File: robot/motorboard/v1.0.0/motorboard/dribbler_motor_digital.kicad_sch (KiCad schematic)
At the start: 13 parts

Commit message: drive and dribbler modules prototype
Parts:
- removed C? (x2): 0.1uF 6.3V, symbol Device:C
- removed C?: 1uF 25V, symbol Device:C
- removed C?: 1uF 6.3V, symbol Device:C
- removed D?: RED, symbol Device:LED
- removed J?: Conn_01x06_Female, symbol Connector:Conn_01x06_Female
- removed J?: Conn_01x05_Female, symbol Connector:Conn_01x05_Female
- removed R?: 1k, symbol Device:R_US
- removed R? (x4): 10k, symbol Device:R_US
- removed U?: STSPIN32F0A, symbol st_microcontrollers:STSPIN32F0A
- added C?: 1uF 25V, symbol Device:C
- added C?: 1uF 6.3V, symbol Device:C
- added C? (x2): 0.1uF 6.3V, symbol Device:C
- added D?: BLUE, symbol Device:LED
- added D?: RED, symbol Device:LED
- added J?: Conn_01x05_Female, symbol Connector:Conn_01x05_Female
- added R? (x4): 10k, symbol Device:R_US
- added R? (x2): 1k, symbol Device:R_US
- added U?: STSPIN32F0A, symbol st_microcontrollers:STSPIN32F0A
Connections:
- net BOOT0: now also U?.42 (BOOT0)
- net GND: now also C?.2, C?.2, C?.2, C?.2, D?.1 (K), D?.1 (K), J?.5 (Pin_5), U?.20 (Test_Mode), U?.44 (GND)
- net HALL_A: now also J?.2 (Pin_2), R?.2, U?.11 (PA0/GPIO/T2C1/ADC0)
- net HALL_B: now also J?.3 (Pin_3), R?.2, U?.12 (PA1/GPIO/T2C2/ADC1)
- net HALL_C: now also J?.4 (Pin_4), R?.2, U?.13 (PA2/GPIO/USART1_TX/T2C3/ADC2)
- net LED_ERR: now also R?.1, U?.41 (PB7/GPIO/USART1_RX)
- net NRST: now also R?.2, U?.7 (NRST)
- net SENSE_U: now also U?.14 (PA3/GPIO/USART1_RX/T2C4/ADC3)
- net SENSE_V: now also U?.15 (PA4/GPIO/ADC4)
- net SENSE_W: now also U?.16 (PA5/GPIO/ADC5)
- net SWDCLK: now also U?.38 (PA14/SWDCLK/USART1_TX/BL_UART_TX)
- net SWDIO: now also U?.37 (PA13/SWDIO)
- net UART_RX: now also U?.39 (PA15/USART1_RX/BL_UART_RX)
- net VDD: now also C?.1, C?.1, R?.1, U?.48 (VDD), U?.9 (SW)
- net VDDA: now also C?.1, U?.10 (VDDA)
- net Vhall: now also J?.1 (Pin_1), R?.1, R?.1, R?.1
- new net: C?.1, U?.6 (VREG12)
- new net: D?.2 (A), R?.2 (x2)
- new net LED_BALL_DET: R?.1, U?.40 (PB6/GPIO/USART1_TX)

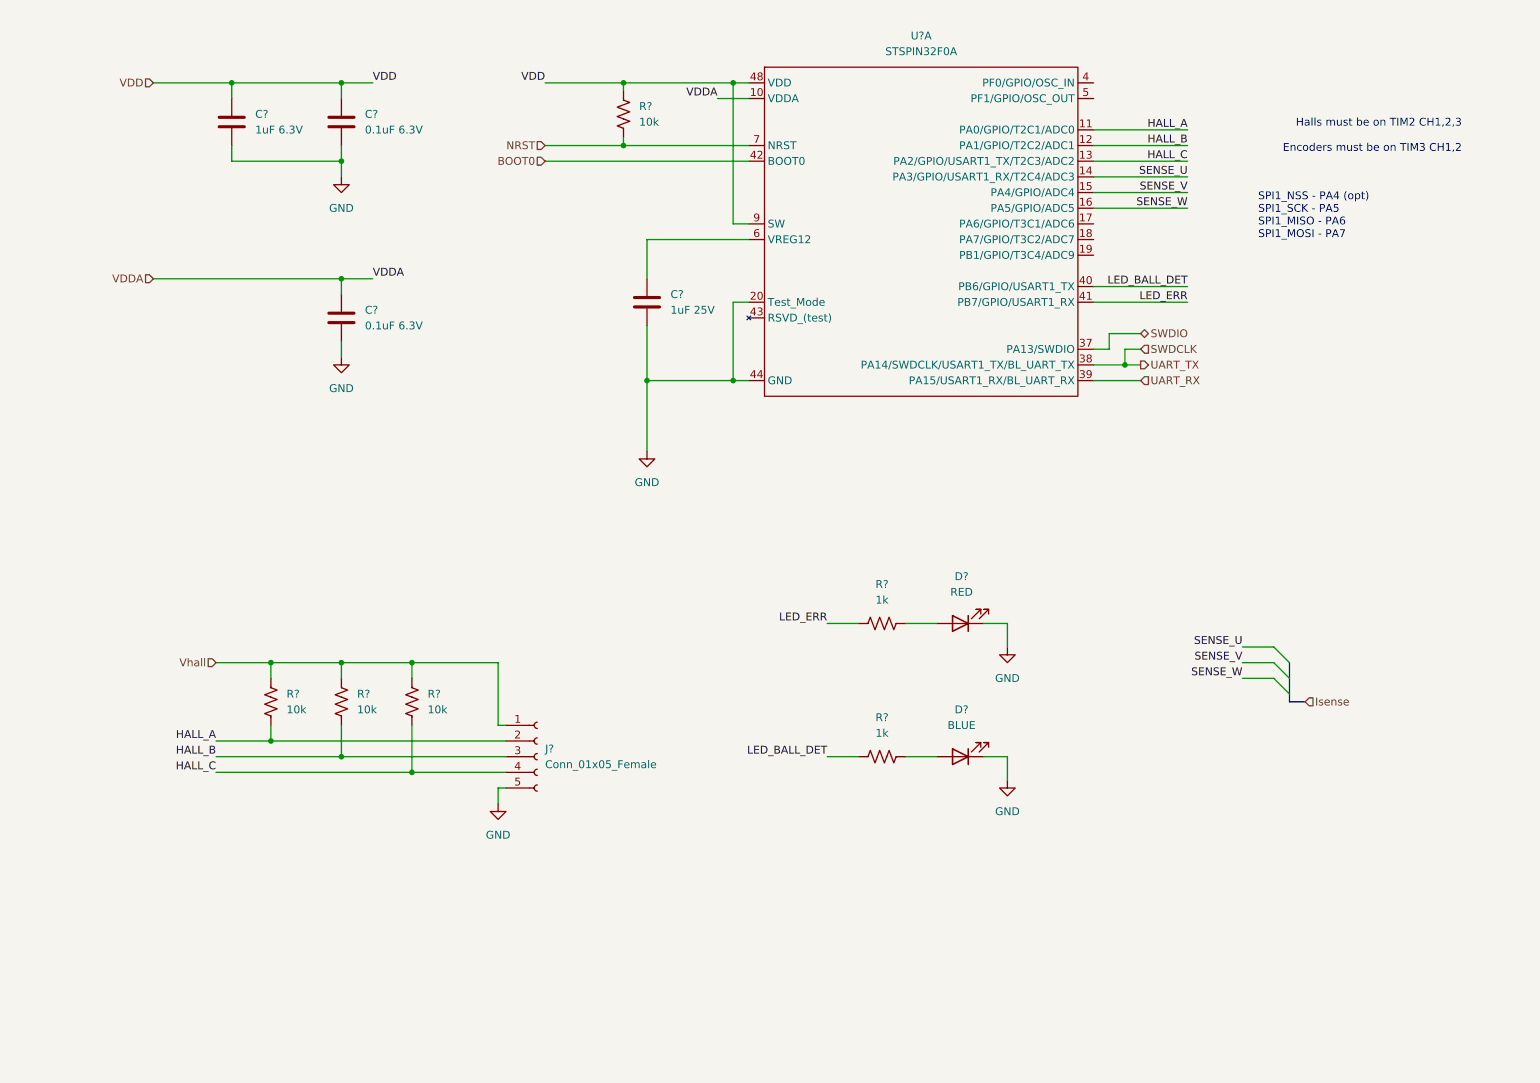
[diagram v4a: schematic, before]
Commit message: bus name ERC fixes
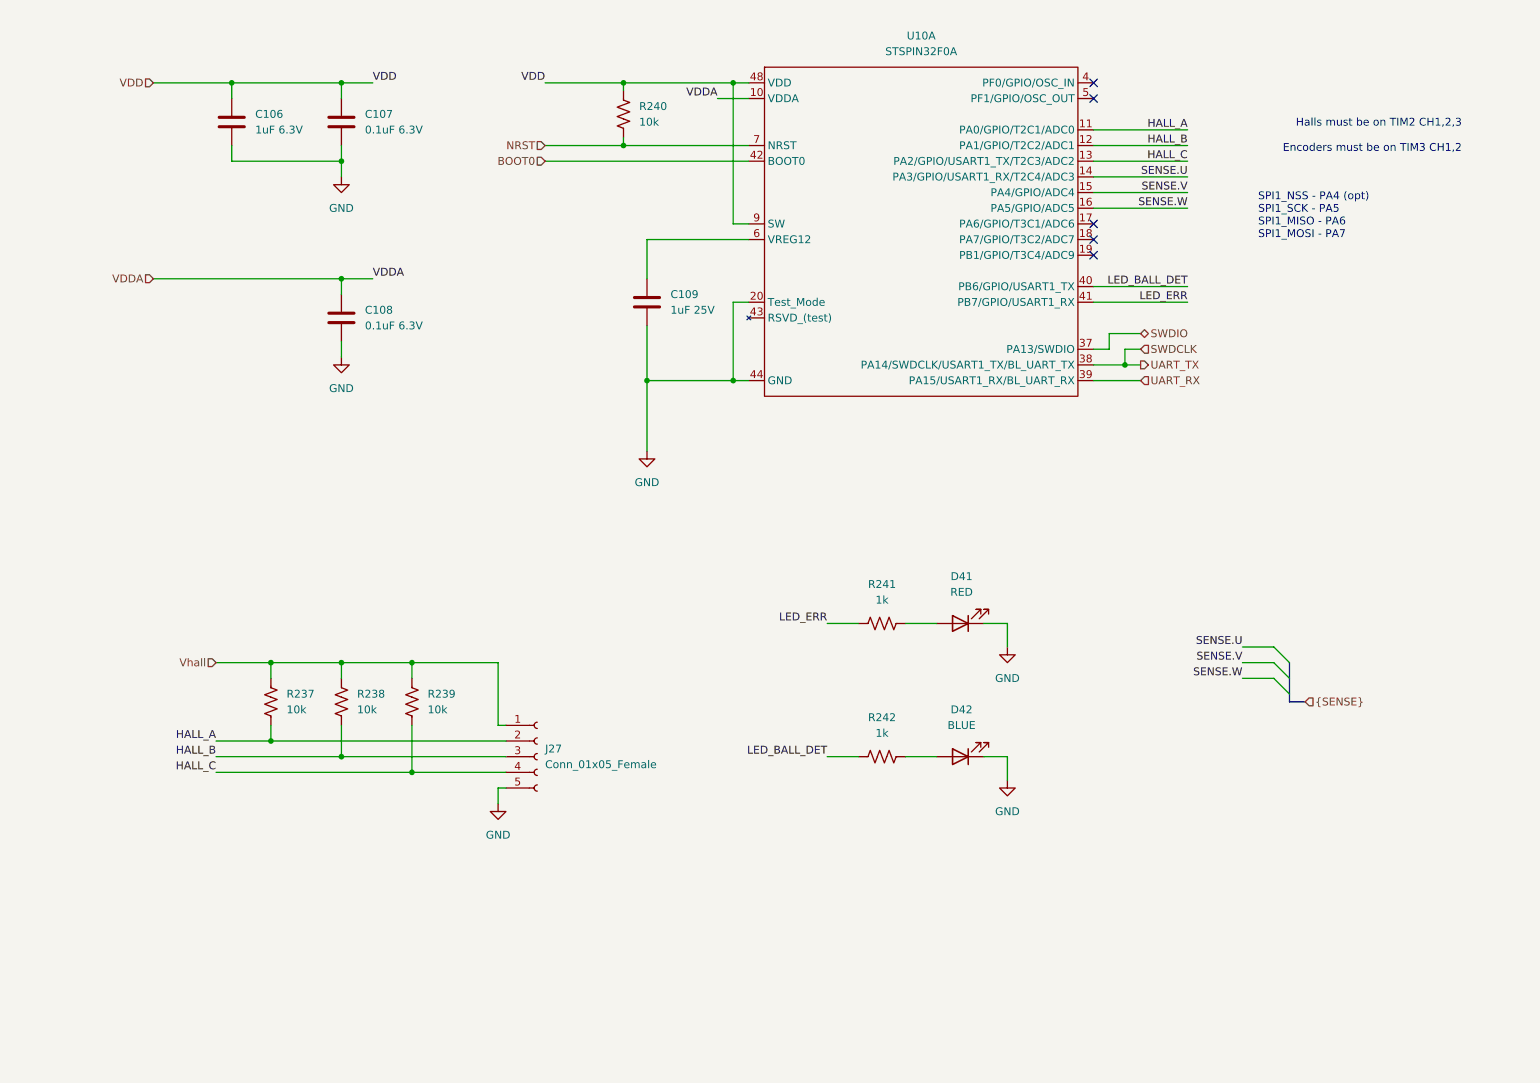
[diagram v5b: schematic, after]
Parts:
- gave numbers to parts that had none: 14
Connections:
- net SENSE_U renamed SENSE.U
- net SENSE_V renamed SENSE.V
- net SENSE_W renamed SENSE.W
- no-connect marks 0 -> 5
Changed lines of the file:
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@@
   (junction (at 135.89 78.74) (diameter 0.9144) (color 0 0 0 0))
   (junction (at 199.39 76.2) (diameter 0.9144) (color 0 0 0 0))
+  (no_connect (at 194.31 30.48))
+  (no_connect (at 194.31 33.02))
+  (no_connect (at 194.31 53.34))
+  (no_connect (at 194.31 55.88))
+  (no_connect (at 194.31 58.42))
   (bus_entry (at 223.52 121.92) (size 2.54 2.54)
     (stroke (width 0) (type solid) (color 0 0 0 0))
@@
     (effects (font (size 1.27 1.27)) (justify right bottom))
   )
-  (label "SENSE_U" (at 209.55 45.72 180)
-    (effects (font (size 1.27 1.27)) (justify right bottom))
-  )
-  (label "SENSE_V" (at 209.55 48.26 180)
-    (effects (font (size 1.27 1.27)) (justify right bottom))
-  )
-  (label "SENSE_W" (at 209.55 50.8 180)
+  (label "SENSE.U" (at 209.55 45.72 180)
+    (effects (font (size 1.27 1.27)) (justify right bottom))
+  )
+  (label "SENSE.V" (at 209.55 48.26 180)
+    (effects (font (size 1.27 1.27)) (justify right bottom))
+  )
+  (label "SENSE.W" (at 209.55 50.8 180)
     (effects (font (size 1.27 1.27)) (justify right bottom))
   )
@@
     (effects (font (size 1.27 1.27)) (justify right bottom))
   )
-  (label "SENSE_U" (at 218.44 121.92 180)
-    (effects (font (size 1.27 1.27)) (justify right bottom))
-  )
-  (label "SENSE_V" (at 218.44 124.46 180)
-    (effects (font (size 1.27 1.27)) (justify right bottom))
-  )
-  (label "SENSE_W" (at 218.44 127 180)
+  (label "SENSE.U" (at 218.44 121.92 180)
+    (effects (font (size 1.27 1.27)) (justify right bottom))
+  )
+  (label "SENSE.V" (at 218.44 124.46 180)
+    (effects (font (size 1.27 1.27)) (justify right bottom))
+  )
+  (label "SENSE.W" (at 218.44 127 180)
     (effects (font (size 1.27 1.27)) (justify right bottom))
   )
@@
     (effects (font (size 1.27 1.27)) (justify left))
   )
-  (hierarchical_label "Isense" (shape input) (at 228.6 130.81 0)
+  (hierarchical_label "{SENSE}" (shape input) (at 228.6 130.81 0)
     (effects (font (size 1.27 1.27)) (justify left))
   )
   (symbol (lib_id "power:GND") (at 72.39 45.72 0) (unit 1)
     (in_bom yes) (on_board yes)
-    (property "Reference" "#PWR?" (id 0) (at 72.39 52.07 0)
+    (property "Reference" "#PWR0160" (id 0) (at 72.39 52.07 0)
       (effects (font (size 1.27 1.27)) hide)
     )
@@
   (symbol (lib_id "power:GND") (at 72.39 74.93 0) (unit 1)
     (in_bom yes) (on_board yes) (fields_autoplaced)
-    (property "Reference" "#PWR?" (id 0) (at 72.39 81.28 0)
+    (property "Reference" "#PWR0161" (id 0) (at 72.39 81.28 0)
       (effects (font (size 1.27 1.27)) hide)
     )
@@
   (symbol (lib_id "power:GND") (at 97.79 147.32 0) (unit 1)
     (in_bom yes) (on_board yes) (fields_autoplaced)
-    (property "Reference" "#PWR?" (id 0) (at 97.79 153.67 0)
+    (property "Reference" "#PWR0162" (id 0) (at 97.79 153.67 0)
       (effects (font (size 1.27 1.27)) hide)
     )
@@
   (symbol (lib_id "power:GND") (at 121.92 90.17 0) (unit 1)
     (in_bom yes) (on_board yes) (fields_autoplaced)
-    (property "Reference" "#PWR?" (id 0) (at 121.92 96.52 0)
+    (property "Reference" "#PWR0163" (id 0) (at 121.92 96.52 0)
       (effects (font (size 1.27 1.27)) hide)
     )
@@
   (symbol (lib_id "power:GND") (at 180.34 121.92 0) (unit 1)
     (in_bom yes) (on_board yes) (fields_autoplaced)
-    (property "Reference" "#PWR?" (id 0) (at 180.34 128.27 0)
+    (property "Reference" "#PWR0164" (id 0) (at 180.34 128.27 0)
       (effects (font (size 1.27 1.27)) hide)
     )
@@
   (symbol (lib_id "power:GND") (at 180.34 143.51 0) (unit 1)
     (in_bom yes) (on_board yes) (fields_autoplaced)
-    (property "Reference" "#PWR?" (id 0) (at 180.34 149.86 0)
+    (property "Reference" "#PWR0165" (id 0) (at 180.34 149.86 0)
       (effects (font (size 1.27 1.27)) hide)
     )
@@
   (symbol (lib_id "Device:R_US") (at 60.96 130.81 0) (unit 1)
     (in_bom yes) (on_board yes) (fields_autoplaced)
-    (property "Reference" "R?" (id 0) (at 63.5 129.5399 0)
+    (property "Reference" "R237" (id 0) (at 63.5 129.5399 0)
       (effects (font (size 1.27 1.27)) (justify left))
     )
@@
   (symbol (lib_id "Device:R_US") (at 72.39 130.81 0) (unit 1)
     (in_bom yes) (on_board yes) (fields_autoplaced)
-    (property "Reference" "R?" (id 0) (at 74.93 129.5399 0)
+    (property "Reference" "R238" (id 0) (at 74.93 129.5399 0)
       (effects (font (size 1.27 1.27)) (justify left))
     )
@@
   (symbol (lib_id "Device:R_US") (at 83.82 130.81 0) (unit 1)
     (in_bom yes) (on_board yes) (fields_autoplaced)
-    (property "Reference" "R?" (id 0) (at 86.36 129.5399 0)
+    (property "Reference" "R239" (id 0) (at 86.36 129.5399 0)
       (effects (font (size 1.27 1.27)) (justify left))
     )
@@
   (symbol (lib_id "Device:R_US") (at 118.11 35.56 0) (unit 1)
     (in_bom yes) (on_board yes) (fields_autoplaced)
-    (property "Reference" "R?" (id 0) (at 120.65 34.2899 0)
+    (property "Reference" "R240" (id 0) (at 120.65 34.2899 0)
       (effects (font (size 1.27 1.27)) (justify left))
     )
@@
   (symbol (lib_id "Device:R_US") (at 160.02 118.11 90) (unit 1)
     (in_bom yes) (on_board yes) (fields_autoplaced)
-    (property "Reference" "R?" (id 0) (at 160.02 111.76 90))
+    (property "Reference" "R241" (id 0) (at 160.02 111.76 90))
     (property "Value" "1k" (id 1) (at 160.02 114.3 90))
     (property "Footprint" "" (id 2) (at 160.274 117.094 90)
@@
   (symbol (lib_id "Device:R_US") (at 160.02 139.7 90) (unit 1)
     (in_bom yes) (on_board yes) (fields_autoplaced)
-    (property "Reference" "R?" (id 0) (at 160.02 133.35 90))
+    (property "Reference" "R242" (id 0) (at 160.02 133.35 90))
     (property "Value" "1k" (id 1) (at 160.02 135.89 90))
     (property "Footprint" "" (id 2) (at 160.274 138.684 90)
@@
   (symbol (lib_id "Device:LED") (at 172.72 118.11 180) (unit 1)
     (in_bom yes) (on_board yes) (fields_autoplaced)
-    (property "Reference" "D?" (id 0) (at 172.9105 110.49 0))
+    (property "Reference" "D41" (id 0) (at 172.9105 110.49 0))
     (property "Value" "RED" (id 1) (at 172.9105 113.03 0))
     (property "Footprint" "" (id 2) (at 172.72 118.11 0)
@@
   (symbol (lib_id "Device:LED") (at 172.72 139.7 180) (unit 1)
     (in_bom yes) (on_board yes) (fields_autoplaced)
-    (property "Reference" "D?" (id 0) (at 172.9105 132.08 0))
+    (property "Reference" "D42" (id 0) (at 172.9105 132.08 0))
     (property "Value" "BLUE" (id 1) (at 172.9105 134.62 0))
     (property "Footprint" "" (id 2) (at 172.72 139.7 0)
@@
   (symbol (lib_id "Device:C") (at 54.61 36.83 0) (unit 1)
     (in_bom yes) (on_board yes) (fields_autoplaced)
-    (property "Reference" "C?" (id 0) (at 58.42 35.5599 0)
+    (property "Reference" "C106" (id 0) (at 58.42 35.5599 0)
       (effects (font (size 1.27 1.27)) (justify left))
     )
@@
   (symbol (lib_id "Device:C") (at 72.39 36.83 0) (unit 1)
     (in_bom yes) (on_board yes) (fields_autoplaced)
-    (property "Reference" "C?" (id 0) (at 76.2 35.5599 0)
+    (property "Reference" "C107" (id 0) (at 76.2 35.5599 0)
       (effects (font (size 1.27 1.27)) (justify left))
     )
@@
   (symbol (lib_id "Device:C") (at 72.39 68.58 0) (unit 1)
     (in_bom yes) (on_board yes) (fields_autoplaced)
-    (property "Reference" "C?" (id 0) (at 76.2 67.3099 0)
+    (property "Reference" "C108" (id 0) (at 76.2 67.3099 0)
       (effects (font (size 1.27 1.27)) (justify left))
     )
@@
   (symbol (lib_id "Device:C") (at 121.92 66.04 0) (unit 1)
     (in_bom yes) (on_board yes) (fields_autoplaced)
-    (property "Reference" "C?" (id 0) (at 125.73 64.7699 0)
+    (property "Reference" "C109" (id 0) (at 125.73 64.7699 0)
       (effects (font (size 1.27 1.27)) (justify left))
     )
@@
   (symbol (lib_id "Connector:Conn_01x05_Female") (at 104.14 139.7 0) (unit 1)
     (in_bom yes) (on_board yes) (fields_autoplaced)
-    (property "Reference" "J?" (id 0) (at 105.41 138.4299 0)
+    (property "Reference" "J27" (id 0) (at 105.41 138.4299 0)
       (effects (font (size 1.27 1.27)) (justify left))
     )
@@
   (symbol (lib_id "st_microcontrollers:STSPIN32F0A") (at 166.37 66.04 0) (unit 1)
     (in_bom yes) (on_board yes) (fields_autoplaced)
-    (property "Reference" "U?" (id 0) (at 166.37 22.86 0))
+    (property "Reference" "U10" (id 0) (at 166.37 22.86 0))
     (property "Value" "STSPIN32F0A" (id 1) (at 166.37 25.4 0))
     (property "Footprint" "" (id 2) (at 168.91 66.04 0)

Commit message: passing ERC
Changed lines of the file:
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@@
+    (stroke (width 0) (type solid) (color 0 0 0 0))
+  )
+  (wire (pts (xy 72.39 59.69) (xy 72.39 62.23))
     (stroke (width 0) (type solid) (color 0 0 0 0))
   )
@@
     (effects (font (size 1.27 1.27)) (justify left))
   )
+  (symbol (lib_id "power:PWR_FLAG") (at 72.39 59.69 0) (unit 1)
+    (in_bom yes) (on_board yes) (fields_autoplaced)
+    (property "Reference" "#FLG016" (id 0) (at 72.39 57.785 0)
+      (effects (font (size 1.27 1.27)) hide)
+    )
+    (property "Value" "PWR_FLAG" (id 1) (at 72.39 54.61 0))
+    (property "Footprint" "" (id 2) (at 72.39 59.69 0)
+      (effects (font (size 1.27 1.27)) hide)
+    )
+    (property "Datasheet" "~" (id 3) (at 72.39 59.69 0)
+      (effects (font (size 1.27 1.27)) hide)
+    )
+    (pin "1")
+  )
   (symbol (lib_id "power:GND") (at 72.39 45.72 0) (unit 1)

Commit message: capacitor footprint assn
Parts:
- C106: value 1uF 6.3V -> 1uF; footprint (none) -> Capacitor_SMD:C_0603_1608Metric_Pad1.08x0.95mm_HandSolder
- C107, C108: value 0.1uF 6.3V -> 0.1uF; footprint (none) -> Capacitor_SMD:C_0402_1005Metric_Pad0.74x0.62mm_HandSolder
- C109: value 1uF 25V -> 1uF; footprint (none) -> Capacitor_SMD:C_0603_1608Metric_Pad1.08x0.95mm_HandSolder
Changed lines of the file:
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@@
       (effects (font (size 1.27 1.27)) (justify left))
     )
-    (property "Value" "1uF 6.3V" (id 1) (at 58.42 38.0999 0)
+    (property "Value" "1uF" (id 1) (at 58.42 38.0999 0)
       (effects (font (size 1.27 1.27)) (justify left))
     )
-    (property "Footprint" "" (id 2) (at 55.5752 40.64 0)
+    (property "Footprint" "Capacitor_SMD:C_0603_1608Metric_Pad1.08x0.95mm_HandSolder" (id 2) (at 55.5752 40.64 0)
       (effects (font (size 1.27 1.27)) hide)
     )
@@
       (effects (font (size 1.27 1.27)) (justify left))
     )
-    (property "Value" "0.1uF 6.3V" (id 1) (at 76.2 38.0999 0)
+    (property "Value" "0.1uF" (id 1) (at 76.2 38.0999 0)
       (effects (font (size 1.27 1.27)) (justify left))
     )
-    (property "Footprint" "" (id 2) (at 73.3552 40.64 0)
+    (property "Footprint" "Capacitor_SMD:C_0402_1005Metric_Pad0.74x0.62mm_HandSolder" (id 2) (at 73.3552 40.64 0)
       (effects (font (size 1.27 1.27)) hide)
     )
@@
       (effects (font (size 1.27 1.27)) (justify left))
     )
-    (property "Value" "0.1uF 6.3V" (id 1) (at 76.2 69.8499 0)
+    (property "Value" "0.1uF" (id 1) (at 76.2 69.8499 0)
       (effects (font (size 1.27 1.27)) (justify left))
     )
-    (property "Footprint" "" (id 2) (at 73.3552 72.39 0)
+    (property "Footprint" "Capacitor_SMD:C_0402_1005Metric_Pad0.74x0.62mm_HandSolder" (id 2) (at 73.3552 72.39 0)
       (effects (font (size 1.27 1.27)) hide)
     )
@@
       (effects (font (size 1.27 1.27)) (justify left))
     )
-    (property "Value" "1uF 25V" (id 1) (at 125.73 67.3099 0)
+    (property "Value" "1uF" (id 1) (at 125.73 67.3099 0)
       (effects (font (size 1.27 1.27)) (justify left))
     )
-    (property "Footprint" "" (id 2) (at 122.8852 69.85 0)
+    (property "Footprint" "Capacitor_SMD:C_0603_1608Metric_Pad1.08x0.95mm_HandSolder" (id 2) (at 122.8852 69.85 0)
       (effects (font (size 1.27 1.27)) hide)
     )
